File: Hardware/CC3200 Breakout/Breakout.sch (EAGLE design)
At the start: 5 parts, among them P1 SSW-110-02-G-D, P2 SSW-110-02-G-D, X1 TSW-105-07-G-S

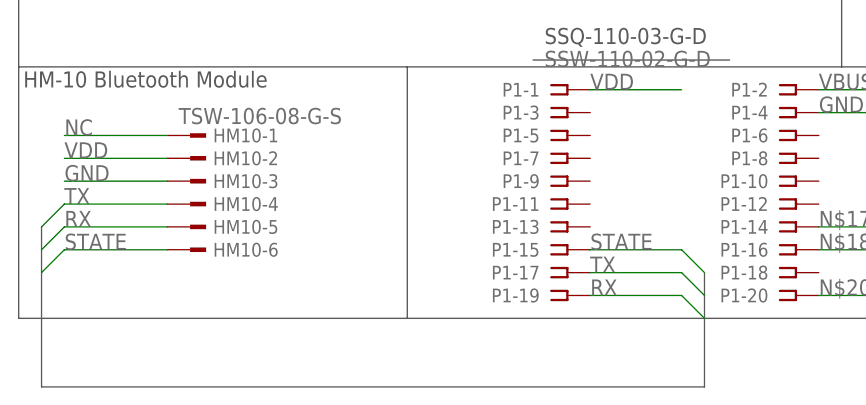
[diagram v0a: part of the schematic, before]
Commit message: Updated the breakout schematics
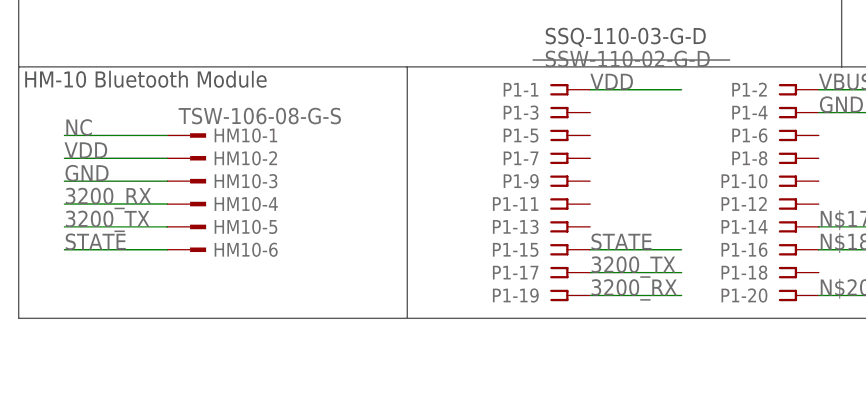
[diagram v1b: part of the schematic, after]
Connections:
- removed net RX: HM10-5.1, P1-19.1
- removed net TX: HM10-4.1, P1-17.1
- new net 3200_RX: HM10-4.1, P1-19.1
- new net 3200_TX: HM10-5.1, P1-17.1
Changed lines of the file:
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@@
 </instances>
 <busses>
-<bus name="UART:RX,STATE,TX">
-<segment>
-<wire x1="5.08" y1="5.08" x2="78.74" y2="5.08" width="0.762" layer="92"/>
-<wire x1="5.08" y1="5.08" x2="5.08" y2="22.86" width="0.762" layer="92"/>
-<wire x1="78.74" y1="5.08" x2="78.74" y2="17.78" width="0.762" layer="92"/>
-</segment>
-</bus>
 </busses>
 <nets>
@@
 </segment>
 </net>
-<net name="TX" class="0">
-<segment>
-<pinref part="HM10" gate="-4" pin="1"/>
-<wire x1="19.05" y1="25.4" x2="7.62" y2="25.4" width="0.1524" layer="91"/>
-<label x="7.62" y="25.4" size="1.778" layer="95"/>
-<wire x1="7.62" y1="25.4" x2="5.08" y2="22.86" width="0.1524" layer="91"/>
-</segment>
-<segment>
-<pinref part="P1" gate="-17" pin="1"/>
-<wire x1="66.04" y1="17.78" x2="76.2" y2="17.78" width="0.1524" layer="91"/>
-<label x="66.04" y="17.78" size="1.778" layer="95"/>
-<wire x1="76.2" y1="17.78" x2="78.74" y2="15.24" width="0.1524" layer="91"/>
-</segment>
-</net>
-<net name="RX" class="0">
-<segment>
-<pinref part="HM10" gate="-5" pin="1"/>
-<wire x1="19.05" y1="22.86" x2="7.62" y2="22.86" width="0.1524" layer="91"/>
-<label x="7.62" y="22.86" size="1.778" layer="95"/>
-<wire x1="7.62" y1="22.86" x2="5.08" y2="20.32" width="0.1524" layer="91"/>
-</segment>
-<segment>
-<pinref part="P1" gate="-19" pin="1"/>
-<wire x1="66.04" y1="15.24" x2="76.2" y2="15.24" width="0.1524" layer="91"/>
-<label x="66.04" y="15.24" size="1.778" layer="95"/>
-<wire x1="76.2" y1="15.24" x2="78.74" y2="12.7" width="0.1524" layer="91"/>
-</segment>
-</net>
 <net name="STATE" class="0">
 <segment>
@@
 <wire x1="19.05" y1="20.32" x2="7.62" y2="20.32" width="0.1524" layer="91"/>
 <label x="7.62" y="20.32" size="1.778" layer="95"/>
-<wire x1="7.62" y1="20.32" x2="5.08" y2="17.78" width="0.1524" layer="91"/>
 </segment>
 <segment>
@@
 <wire x1="66.04" y1="20.32" x2="76.2" y2="20.32" width="0.1524" layer="91"/>
 <label x="66.04" y="20.32" size="1.778" layer="95"/>
-<wire x1="76.2" y1="20.32" x2="78.74" y2="17.78" width="0.1524" layer="91"/>
 </segment>
 </net>
@@
 </segment>
 </net>
+<net name="3200_RX" class="0">
+<segment>
+<pinref part="HM10" gate="-4" pin="1"/>
+<wire x1="19.05" y1="25.4" x2="7.62" y2="25.4" width="0.1524" layer="91"/>
+<label x="7.62" y="25.4" size="1.778" layer="95"/>
+</segment>
+<segment>
+<pinref part="P1" gate="-19" pin="1"/>
+<wire x1="66.04" y1="15.24" x2="76.2" y2="15.24" width="0.1524" layer="91"/>
+<label x="66.04" y="15.24" size="1.778" layer="95"/>
+</segment>
+</net>
+<net name="3200_TX" class="0">
+<segment>
+<pinref part="HM10" gate="-5" pin="1"/>
+<wire x1="19.05" y1="22.86" x2="7.62" y2="22.86" width="0.1524" layer="91"/>
+<label x="7.62" y="22.86" size="1.778" layer="95"/>
+</segment>
+<segment>
+<pinref part="P1" gate="-17" pin="1"/>
+<wire x1="66.04" y1="17.78" x2="76.2" y2="17.78" width="0.1524" layer="91"/>
+<label x="66.04" y="17.78" size="1.778" layer="95"/>
+</segment>
+</net>
